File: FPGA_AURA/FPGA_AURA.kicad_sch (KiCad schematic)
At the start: 0 parts

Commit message: Added AI-generated todo list, started organising repository, and clear goal defined.
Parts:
- added H? (x4): MountingHole_Pad, MountingHole:MountingHole_3.2mm_M3_Pad_Via, symbol Mechanical:MountingHole_Pad
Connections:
- new net GND: H?.1, H?.1, H?.1, H?.1

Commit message: Started pinout after successful Vivado bitstream generation.
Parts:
- gave numbers to parts that had none: 4
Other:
- removed sheet 100_Power_Switching
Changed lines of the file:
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@@
 		(dnp no)
 		(fields_autoplaced yes)
-		(property "Reference" "H?"
+		(property "Reference" "H101"
 			(at 59.69 55.88 90)
 			(show_name no)
@@
 			(project "FPGA_AURA"
 				(path "/3d83cb23-9528-4d06-8969-599520e9eb23"
-					(reference "H?")
+					(reference "H101")
 					(unit 1)
 				)
@@
 		(dnp no)
 		(fields_autoplaced yes)
-		(property "Reference" "H?"
+		(property "Reference" "H103"
 			(at 59.69 68.58 90)
 			(show_name no)
@@
 			(project "FPGA_AURA"
 				(path "/3d83cb23-9528-4d06-8969-599520e9eb23"
-					(reference "H?")
+					(reference "H103")
 					(unit 1)
 				)
@@
 		(dnp no)
 		(fields_autoplaced yes)
-		(property "Reference" "H?"
+		(property "Reference" "H100"
 			(at 46.99 55.88 90)
 			(show_name no)
@@
 			(project "FPGA_AURA"
 				(path "/3d83cb23-9528-4d06-8969-599520e9eb23"
-					(reference "H?")
+					(reference "H100")
 					(unit 1)
 				)
@@
 		(dnp no)
 		(fields_autoplaced yes)
-		(property "Reference" "H?"
+		(property "Reference" "H102"
 			(at 46.99 68.58 90)
 			(show_name no)
@@
 			(project "FPGA_AURA"
 				(path "/3d83cb23-9528-4d06-8969-599520e9eb23"
-					(reference "H?")
+					(reference "H102")
 					(unit 1)
 				)
@@
 				)
 			)
-		)
-	)
-	(sheet
-		(at 22.86 36.83)
-		(size 12.7 12.7)
-		(exclude_from_sim no)
-		(in_bom yes)
-		(on_board yes)
-		(dnp no)
-		(fields_autoplaced yes)
-		(stroke
-			(width 0.1524)
-			(type solid)
-		)
-		(fill
-			(color 0 0 0 0)
-		)
-		(property "Sheetname" "100_Power_Switching"
-			(at 22.86 36.1184 0)
-			(show_name no)
-			(do_not_autoplace no)
-			(effects
-				(font
-					(size 1.27 1.27)
-				)
-				(justify left bottom)
-			)
-		)
-		(property "Sheetfile" "Power_Switching.kicad_sch"
-			(at 22.86 50.1146 0)
-			(hide yes)
-			(show_name no)
-			(do_not_autoplace no)
-			(effects
-				(font
-					(size 1.27 1.27)
-				)
-				(justify left top)
-			)
-		)
-		(instances
-			(project "FPGA_AURA"
-				(path "/3d83cb23-9528-4d06-8969-599520e9eb23"
-					(page "2")
-				)
-			)

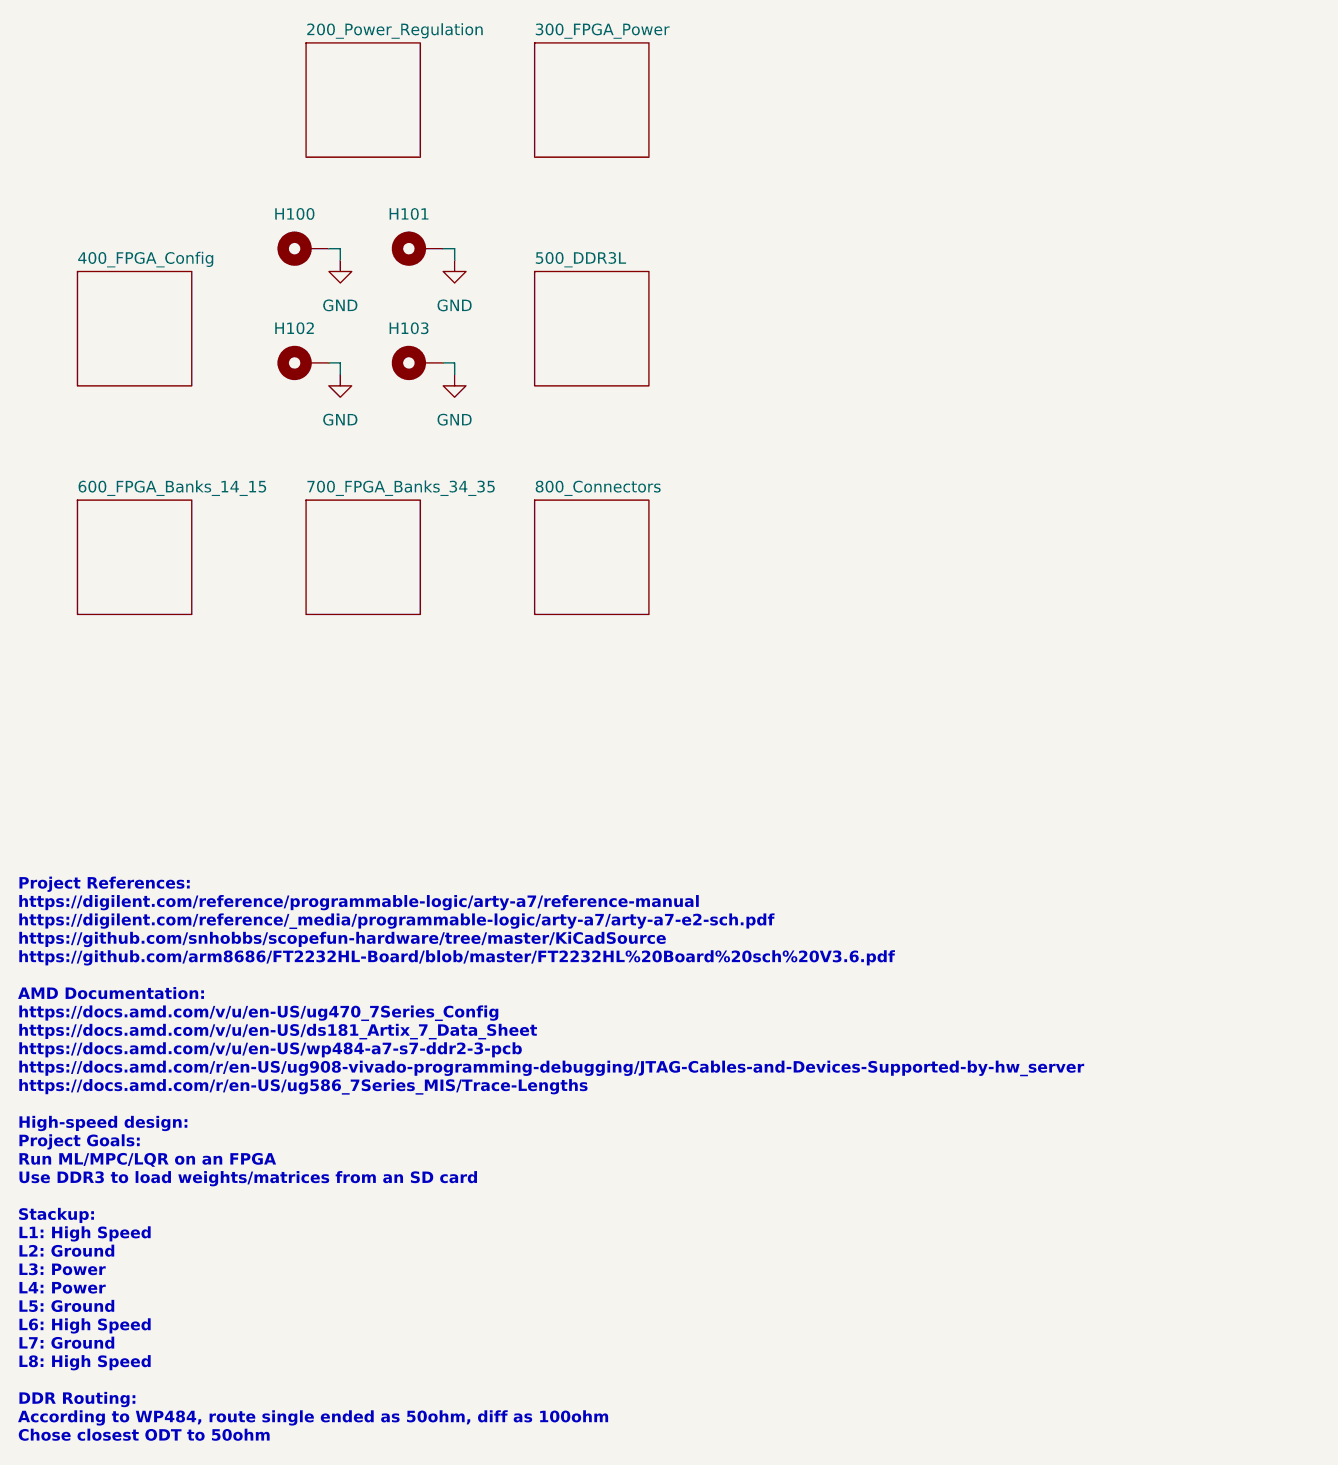
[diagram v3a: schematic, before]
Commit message: Finished schematic to start routing again, and started MII fanout from connector.
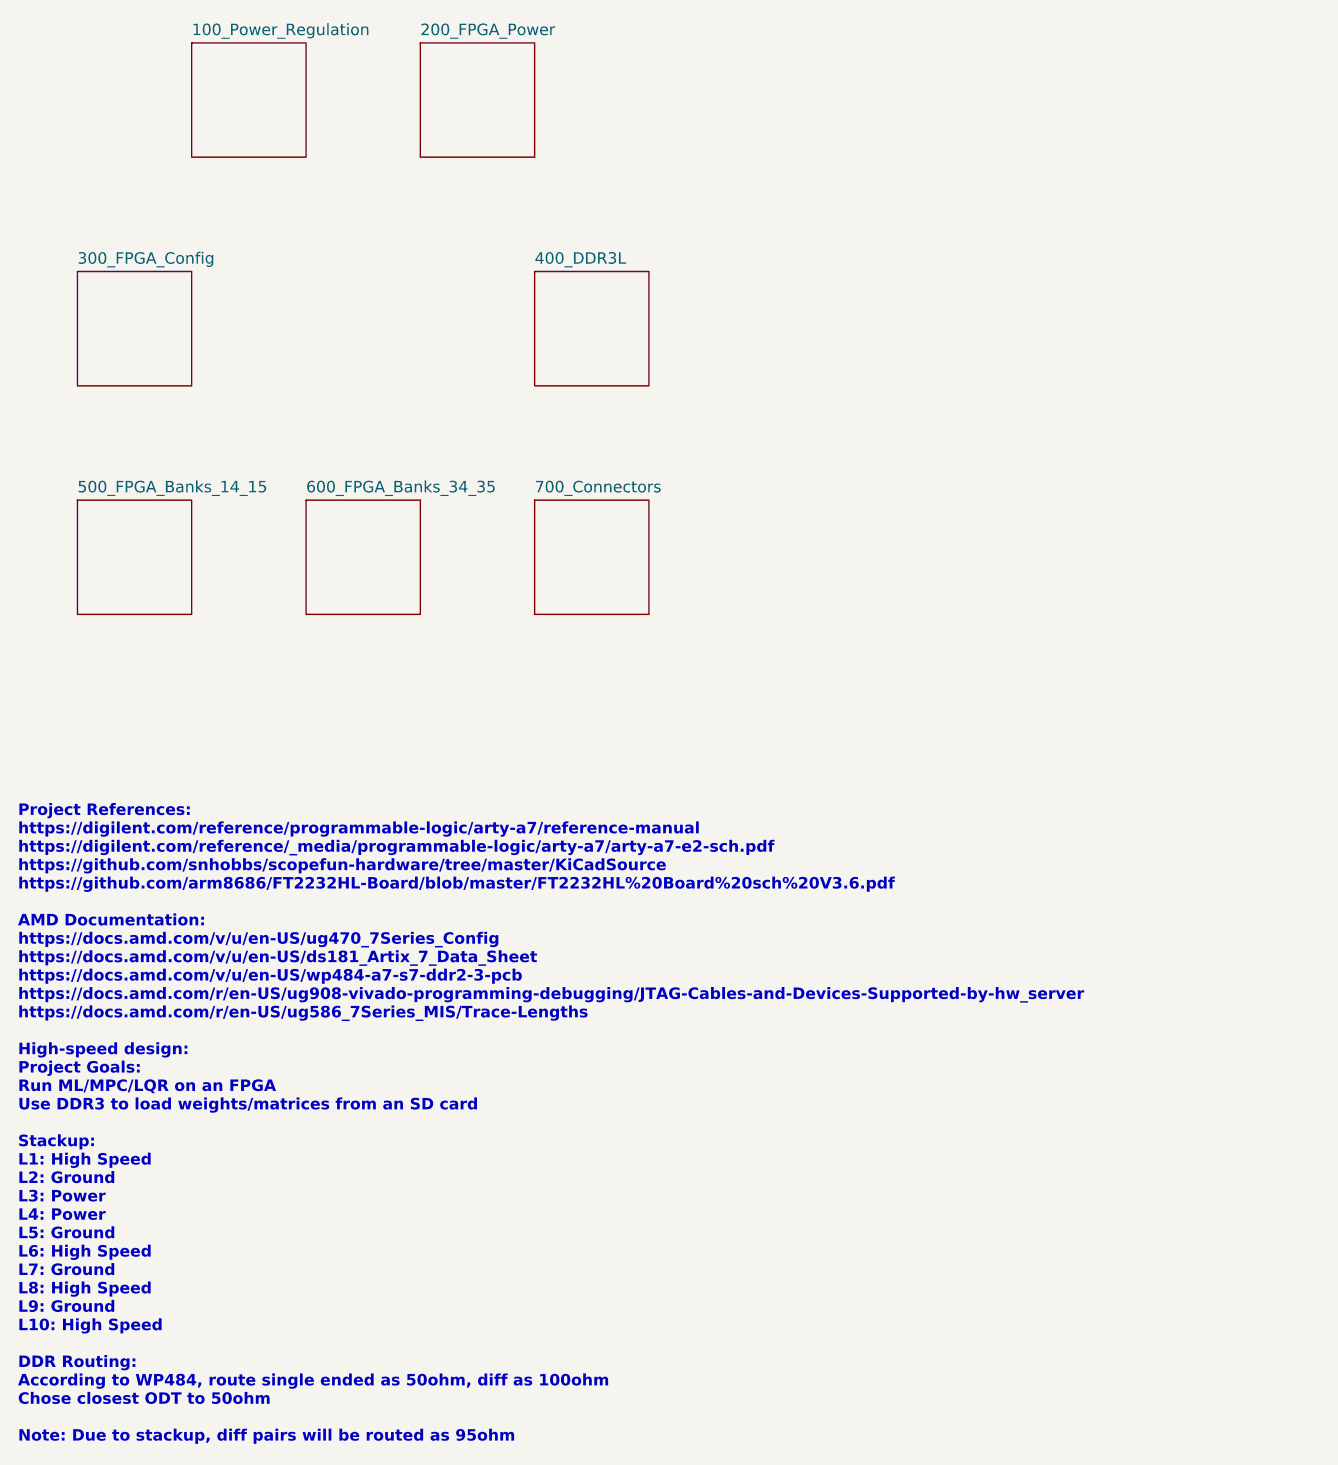
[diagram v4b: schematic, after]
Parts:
- removed H100, H101, H102, H103: MountingHole_Pad, MountingHole:MountingHole_3.2mm_M3_Pad_Via, symbol Mechanical:MountingHole_Pad
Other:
- sheet 200_Power_Regulation renamed 100_Power_Regulation
- sheet 300_FPGA_Power renamed 200_FPGA_Power
- sheet 400_FPGA_Config renamed 300_FPGA_Config
- sheet 500_DDR3L renamed 400_DDR3L
- sheet 600_FPGA_Banks_14_15 renamed 500_FPGA_Banks_14_15
- sheet 700_FPGA_Banks_34_35 renamed 600_FPGA_Banks_34_35
- sheet 800_Connectors renamed 700_Connectors
